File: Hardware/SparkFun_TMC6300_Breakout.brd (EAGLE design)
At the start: 15.2 x 20.3 mm, 56 parts, among them U2 TMC6300

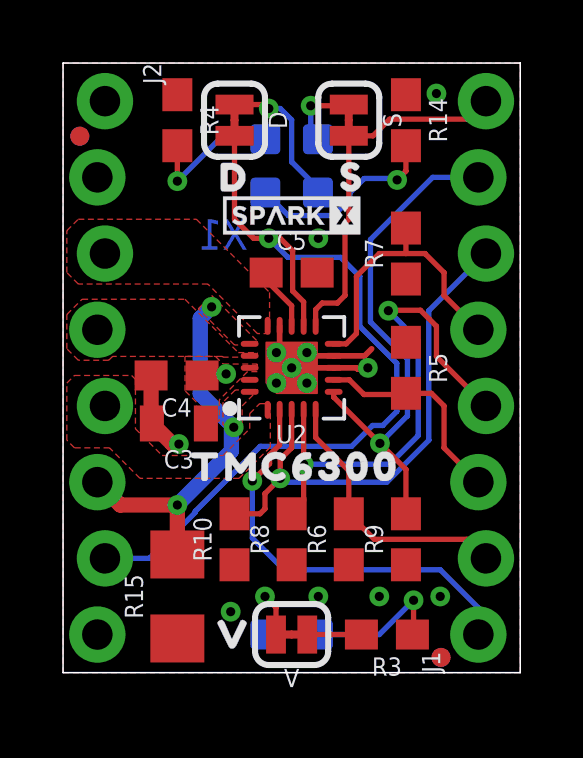
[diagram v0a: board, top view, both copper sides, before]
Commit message: Updates for red review
Added SparkFun logo, updated notes in schematic for user, changed blue LED resistor value, added OSHW logo, created panel and CAM files.
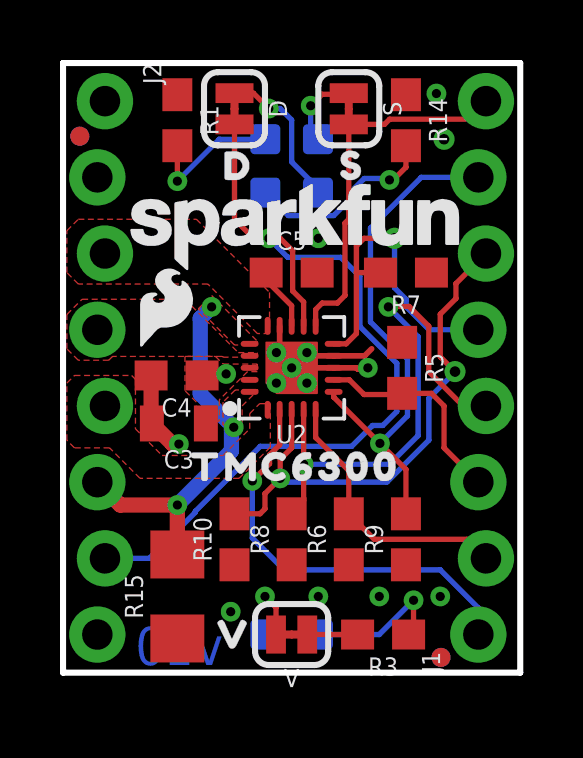
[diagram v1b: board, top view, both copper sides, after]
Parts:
- removed LOGO1: OSHW-LOGONO_SILK, SparkFun-Aesthetics:DUMMY
- removed U$36, U$37: SPARKX-LOGO2, SparkX:SPARKX-TINY
- added LOGO3: SFE_LOGO_NAME.1_INCH, SparkFun-Aesthetics:SFE_LOGO_NAME_.1
- added LOGO4: SFE_LOGO_FLAME.1_INCH, SparkFun-Aesthetics:SFE_LOGO_FLAME_.1
- added LOGO5: OSHW-LOGOS, SparkFun-Aesthetics:OSHW-LOGO-S
- R1: value 330 -> 2.2k
- moved FRAME1 20.3 mm to (-11.4, -31.8)
- moved LOGO2 2.54 mm to (21.6, 50.8)
- moved U$18 2.36 mm to (9.53, 16.0)
- moved U$19 2.29 mm to (9.53, 17.8)
- moved R7 0.63 mm to (11.4, 13.3), turned to 180 degrees
- moved U$16 0.40 mm to (5.84, 16.9)
- moved D 0.38 mm to (5.71, 18.8)
- moved S 0.38 mm to (9.53, 18.8)
- moved U$27 0.38 mm to (9.65, 16.9)
- moved R3 0.13 mm to (10.7, 1.27)
- moved R5 0.13 mm to (11.3, 10.2)
- renumbered R4 to R1
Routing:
- net VL: track 9.53 -> 11.2 mm, vias 0 -> 1
- net UH: track 17.3 -> 17.8 mm, vias 1 -> 2
- net GND: vias 13 -> 14
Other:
- board text added: "Revised by: M. Chodikov"
- board text added: "v10"
- board text removed: "X1"

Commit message: Changes made from design notes
Changed vias to be all the same size, added paragraphs to S and D jumpers to explain what they're going to, added tRestrict layer to remove natural jumper between GND pads, fixed acid trap, added more GND vias for better heat sinking.
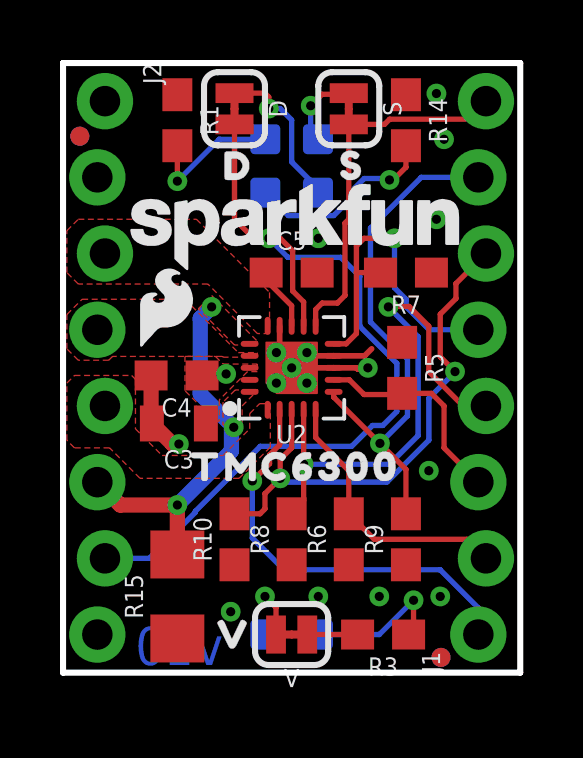
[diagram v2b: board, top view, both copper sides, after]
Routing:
- net GND: vias 14 -> 16
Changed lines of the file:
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@@
 <drawing>
 <settings>
-<setting alwaysvectorfont="yes"/>
+<setting alwaysvectorfont="no"/>
 <setting verticaltext="up"/>
 </settings>
@@
 <layer number="39" name="tKeepout" color="4" fill="11" visible="no" active="yes"/>
 <layer number="40" name="bKeepout" color="1" fill="11" visible="no" active="yes"/>
-<layer number="41" name="tRestrict" color="4" fill="10" visible="no" active="yes"/>
+<layer number="41" name="tRestrict" color="4" fill="10" visible="yes" active="yes"/>
 <layer number="42" name="bRestrict" color="1" fill="10" visible="no" active="yes"/>
 <layer number="43" name="vRestrict" color="2" fill="10" visible="no" active="yes"/>
@@
 <dimension x1="5.842" y1="8.509" x2="0" y2="8.509" x3="2.921" y3="-19.05" textsize="1.778" layer="49" unit="inch"/>
 <dimension x1="1.27" y1="1.27" x2="0" y2="1.27" x3="0.635" y3="-3.81" textsize="1.778" layer="47" unit="inch"/>
+<polygon width="0.1524" layer="41">
+<vertex x="8.89" y="10.033"/>
+<vertex x="9.271" y="10.033"/>
+<vertex x="9.271" y="10.668"/>
+<vertex x="8.763" y="10.668"/>
+<vertex x="8.763" y="10.033"/>
+</polygon>
 </plain>
 <attributes>
@@
 <contactref element="J2" pad="2"/>
 <contactref element="J2" pad="8"/>
-<via x="12.7" y="17.78" extent="1-16" drill="0.35"/>
+<via x="12.7" y="17.78" extent="1-16" drill="0.3048"/>
 <contactref element="R1" pad="1"/>
+<via x="12.446" y="15.113" extent="1-16" drill="0.3048"/>
+<via x="12.192" y="6.731" extent="1-16" drill="0.3048"/>
 </signal>
 <signal name="N$1">
@@
 <wire x1="9.779" y1="11.303" x2="9.779" y2="13.335" width="0.1778" layer="1"/>
 <wire x1="9.779" y1="13.335" x2="9.779" y2="14.224" width="0.1778" layer="1"/>
-<via x="11.049" y="14.478" extent="1-16" drill="0.35"/>
+<via x="11.049" y="14.478" extent="1-16" drill="0.3048"/>
 <wire x1="10.033" y1="14.478" x2="11.049" y2="14.478" width="0.1778" layer="1"/>
 <wire x1="10.58" y1="13.335" x2="9.779" y2="13.335" width="0.1778" layer="1"/>
@@
 <wire x1="12.192" y1="7.747" x2="12.192" y2="9.144" width="0.1778" layer="16"/>
 <wire x1="13.0655" y1="10.0175" x2="13.0655" y2="10.03560625" width="0.1778" layer="16"/>
-<via x="13.0655" y="10.03560625" extent="1-16" drill="0.35"/>
+<via x="13.0655" y="10.03560625" extent="1-16" drill="0.3048"/>
 <wire x1="12.192" y1="9.144" x2="13.0655" y2="10.0175" width="0.1778" layer="16"/>
 <wire x1="13.0655" y1="10.03560625" x2="12.573" y2="10.52810625" width="0.1778" layer="1"/>
@@
 <wire x1="7.62" y1="17.02645" x2="8.497" y2="16.14945" width="0.1778" layer="16"/>
 <via x="6.858" y="18.80445" extent="1-16" drill="0.3048"/>
-<wire x1="6.858" y1="18.80445" x2="6.34575" y2="19.3167" width="0.1778" layer="1"/>
-<wire x1="5.715" y1="19.3167" x2="6.34575" y2="19.3167" width="0.1778" layer="1"/>
+<wire x1="6.858" y1="18.80445" x2="6.858" y2="19.18545" width="0.1778" layer="1"/>
+<wire x1="6.858" y1="19.18545" x2="6.72675" y2="19.3167" width="0.1778" layer="1"/>
+<wire x1="5.715" y1="19.3167" x2="6.72675" y2="19.3167" width="0.1778" layer="1"/>
 </signal>
 <signal name="N$5">
